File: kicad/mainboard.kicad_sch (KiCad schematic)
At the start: 1 part, among them U1 4051

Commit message: Added all 5041
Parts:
- added U2, U3, U4, U5, U6, U7, U8: 4051, symbol 4xxx:4051
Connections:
- net +5V: now also U2.16 (VDD), U3.16 (VDD), U4.16 (VDD), U5.16 (VDD), U6.16 (VDD), U7.16 (VDD), U8.16 (VDD)
- net -5V: now also U2.8 (VSS), U3.8 (VSS), U4.8 (VSS), U5.8 (VSS), U6.8 (VSS), U7.8 (VSS), U8.8 (VSS)
- net GND: now also U2.7 (VEE), U3.7 (VEE), U4.7 (VEE), U5.7 (VEE), U6.7 (VEE), U7.7 (VEE), U8.7 (VEE)
- net OUT1: now also U2.13 (X0), U3.13 (X0), U4.13 (X0), U5.13 (X0), U6.13 (X0), U7.13 (X0), U8.13 (X0)
- net OUT2: now also U2.14 (X1), U3.14 (X1), U4.14 (X1), U5.14 (X1), U6.14 (X1), U7.14 (X1), U8.14 (X1)
- net OUT3: now also U2.15 (X2), U3.15 (X2), U4.15 (X2), U5.15 (X2), U6.15 (X2), U7.15 (X2), U8.15 (X2)
- net OUT4: now also U2.12 (X3), U3.12 (X3), U4.12 (X3), U5.12 (X3), U6.12 (X3), U7.12 (X3), U8.12 (X3)
- net OUT5: now also U2.1 (X4), U3.1 (X4), U4.1 (X4), U5.1 (X4), U6.1 (X4), U7.1 (X4), U8.1 (X4)
- net OUT6: now also U2.5 (X5), U3.5 (X5), U4.5 (X5), U5.5 (X5), U6.5 (X5), U7.5 (X5), U8.5 (X5)
- net OUT7: now also U2.2 (X6), U3.2 (X6), U4.2 (X6), U5.2 (X6), U6.2 (X6), U7.2 (X6), U8.2 (X6)
- net OUT8: now also U2.4 (X7), U3.4 (X7), U4.4 (X7), U5.4 (X7), U6.4 (X7), U7.4 (X7), U8.4 (X7)
- net IO1B: now reaches U1.10 (B)
- net IO1A: now reaches U1.11 (A)
- net IO1OE: now reaches U1.6 (Inh)
- net IO1C: now reaches U1.9 (C)
- new net IN2: U2.3 (X)
- new net IN3: U3.3 (X)
- new net IN4: U4.3 (X)
- new net IN5: U5.3 (X)
- new net IN6: U6.3 (X)
- new net IN7: U7.3 (X)
- new net IN8: U8.3 (X)
- new net IO2A: U2.11 (A)
- new net IO2B: U2.10 (B)
- new net IO2C: U2.9 (C)
- new net IO2OE: U2.6 (Inh)
- new net IO3A: U3.11 (A)
- new net IO3B: U3.10 (B)
- new net IO3C: U3.9 (C)
- new net IO3OE: U3.6 (Inh)
- new net IO4A: U4.11 (A)
- new net IO4B: U4.10 (B)
- new net IO4C: U4.9 (C)
- new net IO4OE: U4.6 (Inh)
- new net IO5A: U5.11 (A)
- new net IO5B: U5.10 (B)
- new net IO5C: U5.9 (C)
- new net IO5OE: U5.6 (Inh)
- new net IO6A: U6.11 (A)
- new net IO6B: U6.10 (B)
- new net IO6C: U6.9 (C)
- new net IO6OE: U6.6 (Inh)
- new net IO7A: U7.11 (A)
- new net IO7B: U7.10 (B)
- new net IO7C: U7.9 (C)
- new net IO7OE: U7.6 (Inh)
- new net IO8A: U8.11 (A)
- new net IO8B: U8.10 (B)
- new net IO8C: U8.9 (C)
- new net IO8OE: U8.6 (Inh)
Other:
- moved on the sheet: U1

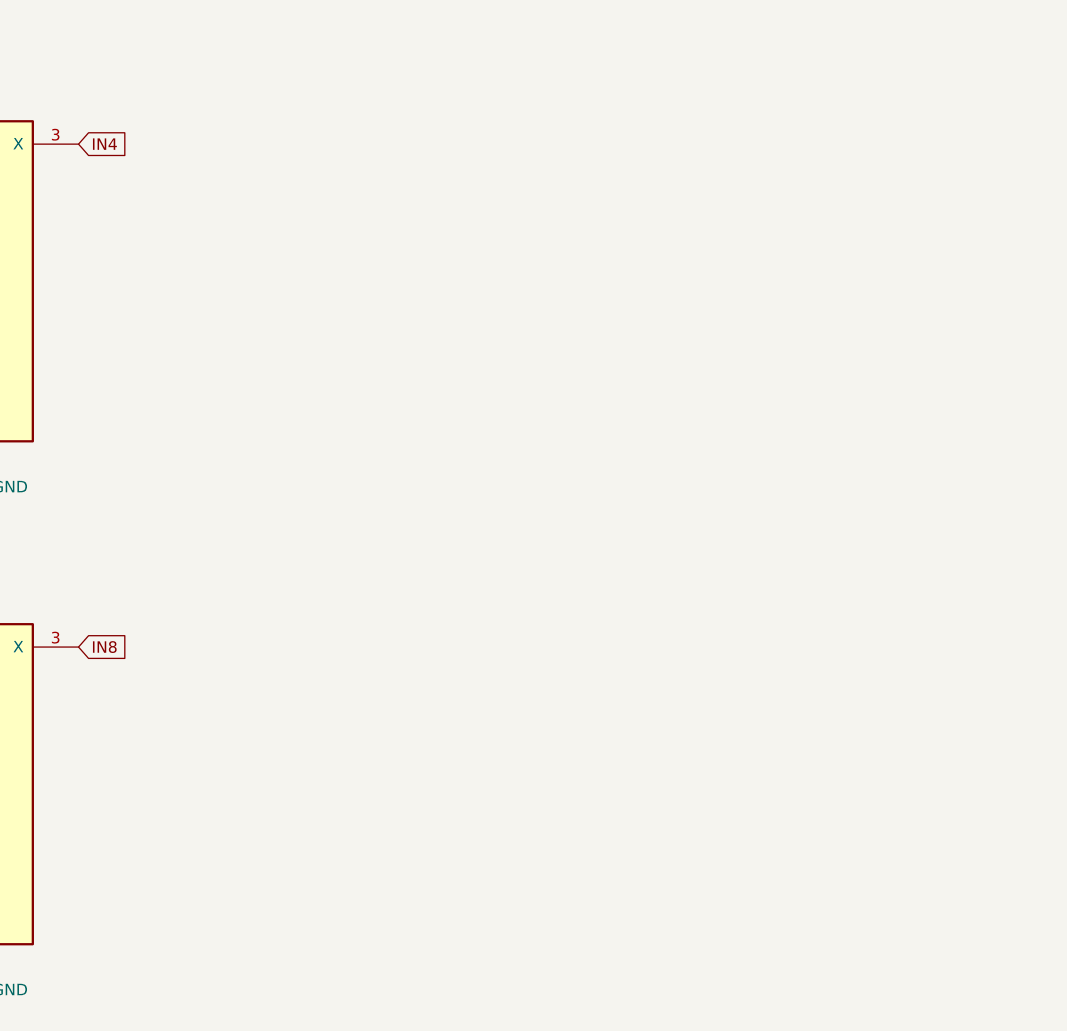
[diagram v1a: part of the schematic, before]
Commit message: Added data latches
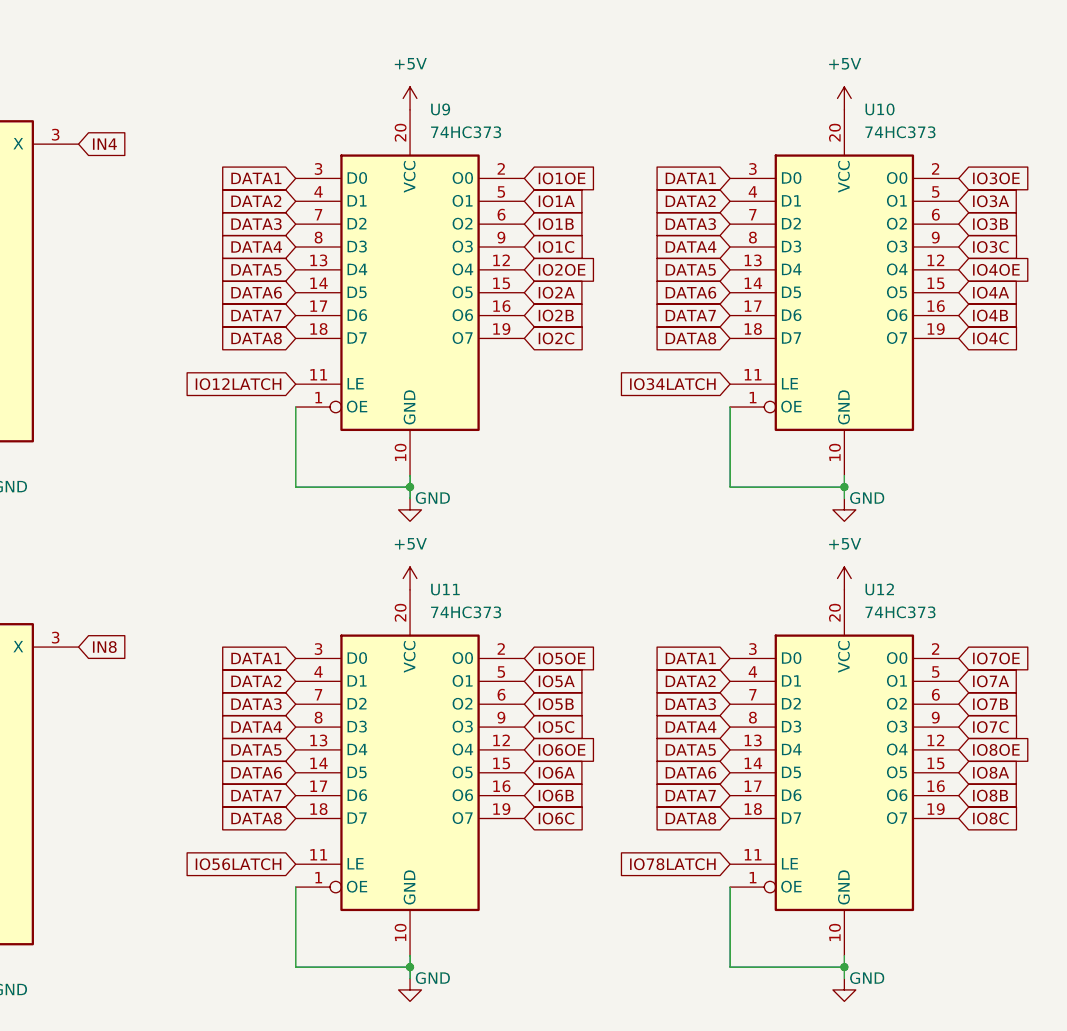
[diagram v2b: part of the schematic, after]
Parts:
- added U10, U11, U12, U9: 74HC373, symbol 74xx:74HC373
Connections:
- net +5V: now also U10.20 (VCC), U11.20 (VCC), U12.20 (VCC), U9.20 (VCC)
- net GND: now also U10.1 (OE), U10.10 (GND), U11.1 (OE), U11.10 (GND), U12.1 (OE), U12.10 (GND), U9.1 (OE), U9.10 (GND)
- net IO1A: now also U9.5 (O1)
- net IO1B: now also U9.6 (O2)
- net IO1C: now also U9.9 (O3)
- net IO1OE: now also U9.2 (O0)
- net IO2A: now also U9.15 (O5)
- net IO2B: now also U9.16 (O6)
- net IO2C: now also U9.19 (O7)
- net IO2OE: now also U9.12 (O4)
- net IO3A: now also U10.5 (O1)
- net IO3B: now also U10.6 (O2)
- net IO3C: now also U10.9 (O3)
- net IO3OE: now also U10.2 (O0)
- net IO4A: now also U10.15 (O5)
- net IO4B: now also U10.16 (O6)
- net IO4C: now also U10.19 (O7)
- net IO4OE: now also U10.12 (O4)
- net IO5A: now also U11.5 (O1)
- net IO5B: now also U11.6 (O2)
- net IO5C: now also U11.9 (O3)
- net IO5OE: now also U11.2 (O0)
- net IO6A: now also U11.15 (O5)
- net IO6B: now also U11.16 (O6)
- net IO6C: now also U11.19 (O7)
- net IO6OE: now also U11.12 (O4)
- net IO7A: now also U12.5 (O1)
- net IO7B: now also U12.6 (O2)
- net IO7C: now also U12.9 (O3)
- net IO7OE: now also U12.2 (O0)
- net IO8A: now also U12.15 (O5)
- net IO8B: now also U12.16 (O6)
- net IO8C: now also U12.19 (O7)
- net IO8OE: now also U12.12 (O4)
- new net DATA1: U10.3 (D0), U11.3 (D0), U12.3 (D0), U9.3 (D0)
- new net DATA2: U10.4 (D1), U11.4 (D1), U12.4 (D1), U9.4 (D1)
- new net DATA3: U10.7 (D2), U11.7 (D2), U12.7 (D2), U9.7 (D2)
- new net DATA4: U10.8 (D3), U11.8 (D3), U12.8 (D3), U9.8 (D3)
- new net DATA5: U10.13 (D4), U11.13 (D4), U12.13 (D4), U9.13 (D4)
- new net DATA6: U10.14 (D5), U11.14 (D5), U12.14 (D5), U9.14 (D5)
- new net DATA7: U10.17 (D6), U11.17 (D6), U12.17 (D6), U9.17 (D6)
- new net DATA8: U10.18 (D7), U11.18 (D7), U12.18 (D7), U9.18 (D7)
- new net IO12LATCH: U9.11 (LE)
- new net IO34LATCH: U10.11 (LE)
- new net IO56LATCH: U11.11 (LE)
- new net IO78LATCH: U12.11 (LE)

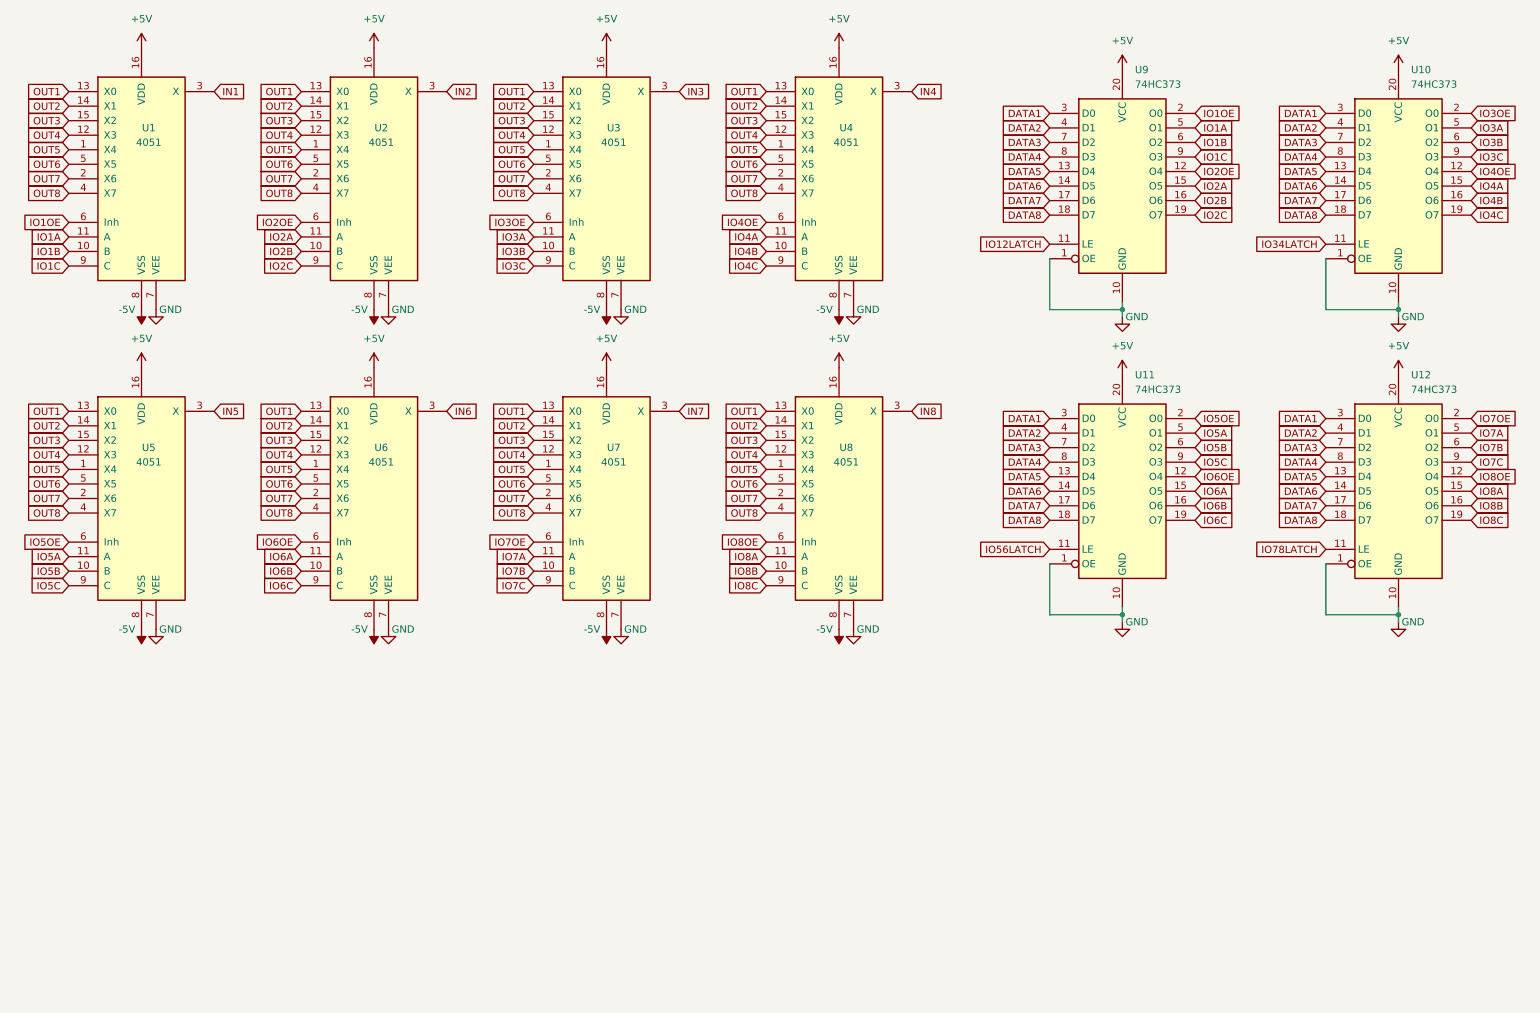
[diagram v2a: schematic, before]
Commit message: Scetch of pcb. Uses 74595 for now which is bit slow
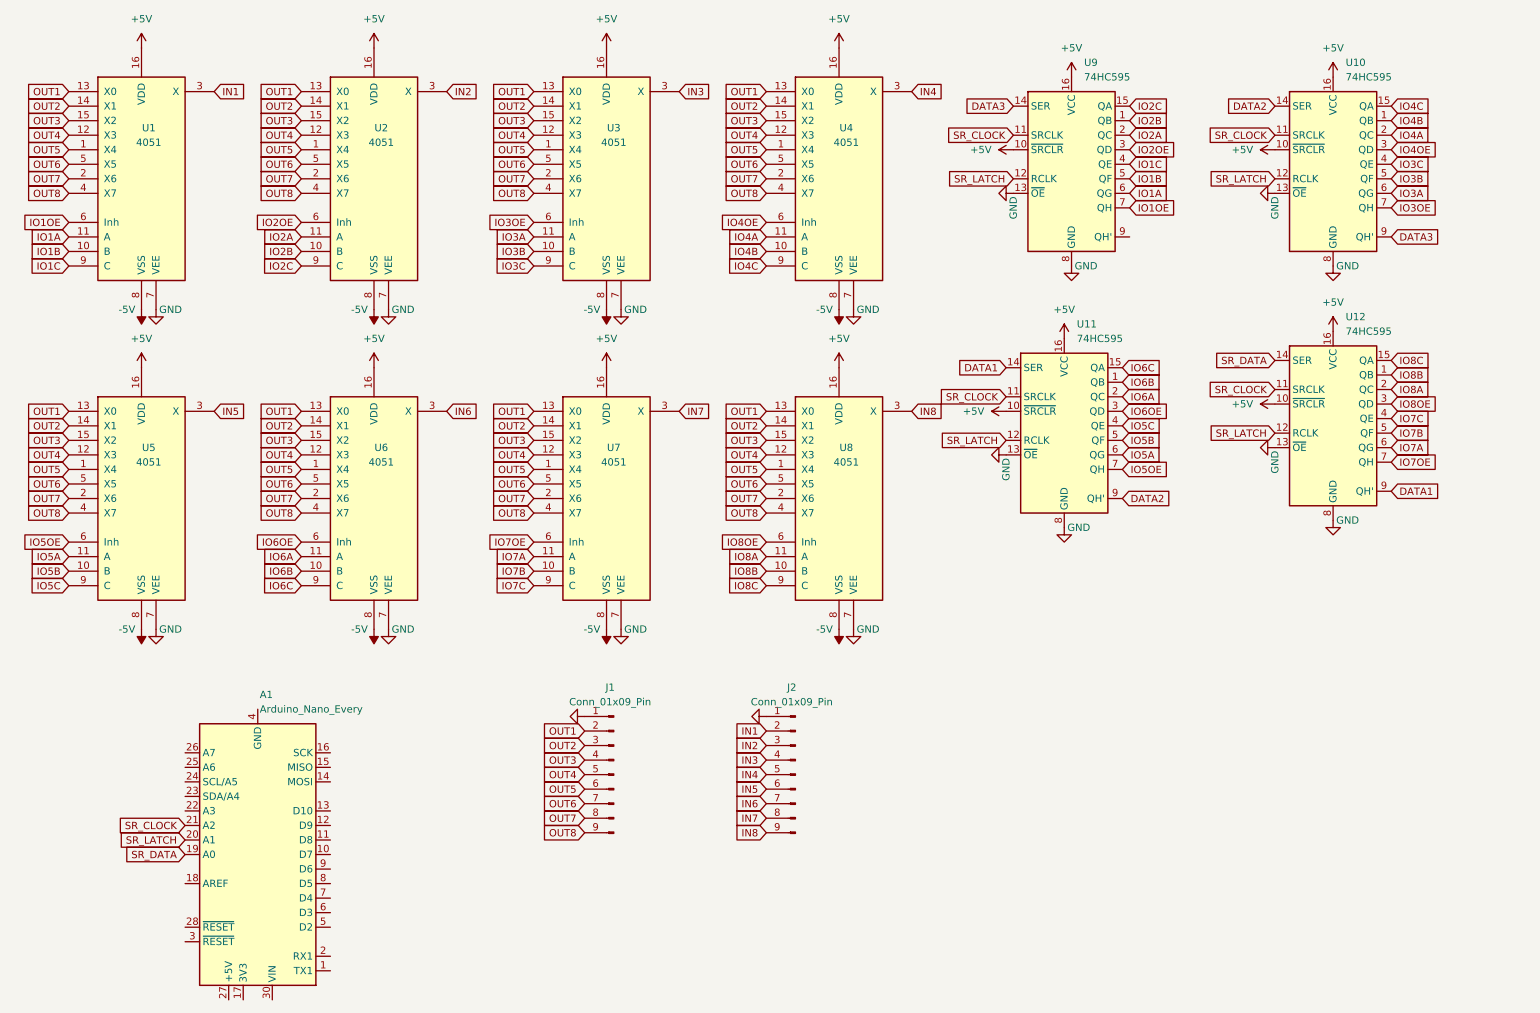
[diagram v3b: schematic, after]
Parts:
- removed U10, U11, U12, U9: 74HC373, symbol 74xx:74HC373
- added A1: Arduino_Nano_Every, Module:Arduino_Nano, symbol MCU_Module:Arduino_Nano_Every
- added J1, J2: Conn_01x09_Pin, Connector_PinHeader_2.54mm:PinHeader_2x05_P2.54mm_Vertical, symbol Connector:Conn_01x09_Pin
- added U10, U11, U12, U9: 74HC595, Package_DIP:DIP-16_W7.62mm_Socket_LongPads, symbol 74xx:74HC595
- U1, U2, U3, U4, U5, U6, U7, U8: footprint (none) -> Package_DIP:DIP-16_W7.62mm_Socket_LongPads
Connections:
- net +5V: now also U10.10 (~{SRCLR}), U10.16 (VCC), U11.10 (~{SRCLR}), U11.16 (VCC), U12.10 (~{SRCLR}), U12.16 (VCC), U9.10 (~{SRCLR}), U9.16 (VCC)
- net DATA1: now also U11.14 (SER), U12.9 (QH')
- net DATA2: now also U10.14 (SER), U11.9 (QH')
- net DATA3: now also U10.9 (QH'), U9.14 (SER)
- net GND: now also J1.1 (Pin_1), J2.1 (Pin_1), U10.13 (~{OE}), U10.8 (GND), U11.13 (~{OE}), U11.8 (GND), U12.13 (~{OE}), U12.8 (GND), U9.13 (~{OE}), U9.8 (GND)
- net IN1: now also J2.2 (Pin_2)
- net IN2: now also J2.3 (Pin_3)
- net IN3: now also J2.4 (Pin_4)
- net IN4: now also J2.5 (Pin_5)
- net IN5: now also J2.6 (Pin_6)
- net IN6: now also J2.7 (Pin_7)
- net IN7: now also J2.8 (Pin_8)
- net IN8: now also J2.9 (Pin_9)
- net IO1A: now also U9.6 (QG)
- net IO1B: now also U9.5 (QF)
- net IO1C: now also U9.4 (QE)
- net IO1OE: now also U9.7 (QH)
- net IO2A: now also U9.2 (QC)
- net IO2B: now also U9.1 (QB)
- net IO2C: now also U9.15 (QA)
- net IO2OE: now also U9.3 (QD)
- net IO3A: now also U10.6 (QG)
- net IO3B: now also U10.5 (QF)
- net IO3C: now also U10.4 (QE)
- net IO3OE: now also U10.7 (QH)
- net IO4A: now also U10.2 (QC)
- net IO4B: now also U10.1 (QB)
- net IO4C: now also U10.15 (QA)
- net IO4OE: now also U10.3 (QD)
- net IO5A: now also U11.6 (QG)
- net IO5B: now also U11.5 (QF)
- net IO5C: now also U11.4 (QE)
- net IO5OE: now also U11.7 (QH)
- net IO6A: now also U11.2 (QC)
- net IO6B: now also U11.1 (QB)
- net IO6C: now also U11.15 (QA)
- net IO6OE: now also U11.3 (QD)
- net IO7A: now also U12.6 (QG)
- net IO7B: now also U12.5 (QF)
- net IO7C: now also U12.4 (QE)
- net IO7OE: now also U12.7 (QH)
- net IO8A: now also U12.2 (QC)
- net IO8B: now also U12.1 (QB)
- net IO8C: now also U12.15 (QA)
- net IO8OE: now also U12.3 (QD)
- net OUT1: now also J1.2 (Pin_2)
- net OUT2: now also J1.3 (Pin_3)
- net OUT3: now also J1.4 (Pin_4)
- net OUT4: now also J1.5 (Pin_5)
- net OUT5: now also J1.6 (Pin_6)
- net OUT6: now also J1.7 (Pin_7)
- net OUT7: now also J1.8 (Pin_8)
- net OUT8: now also J1.9 (Pin_9)
- new net: A1.29 (GND), A1.4 (GND)
- new net SR_CLOCK: A1.21 (A2), U10.11 (SRCLK), U11.11 (SRCLK), U12.11 (SRCLK), U9.11 (SRCLK)
- new net SR_DATA: A1.19 (A0), U12.14 (SER)
- new net SR_LATCH: A1.20 (A1), U10.12 (RCLK), U11.12 (RCLK), U12.12 (RCLK), U9.12 (RCLK)
